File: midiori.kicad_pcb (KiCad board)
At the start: 2 copper layers, 140 x 150 mm, 47 parts, among them J1 x68000_expansion, J2 Conn_ARM_JTAG_SWD_10, J3 DIN-5_180degree, J4 Conn_02x03_Odd_Even, J7 AudioJack3, U1 74LCX07, U10 ICE40HX1K-VQ100, U11 TLV73333PDBV, U2 AT25SF081-SSHD-X, U3 TLV73312PDBV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

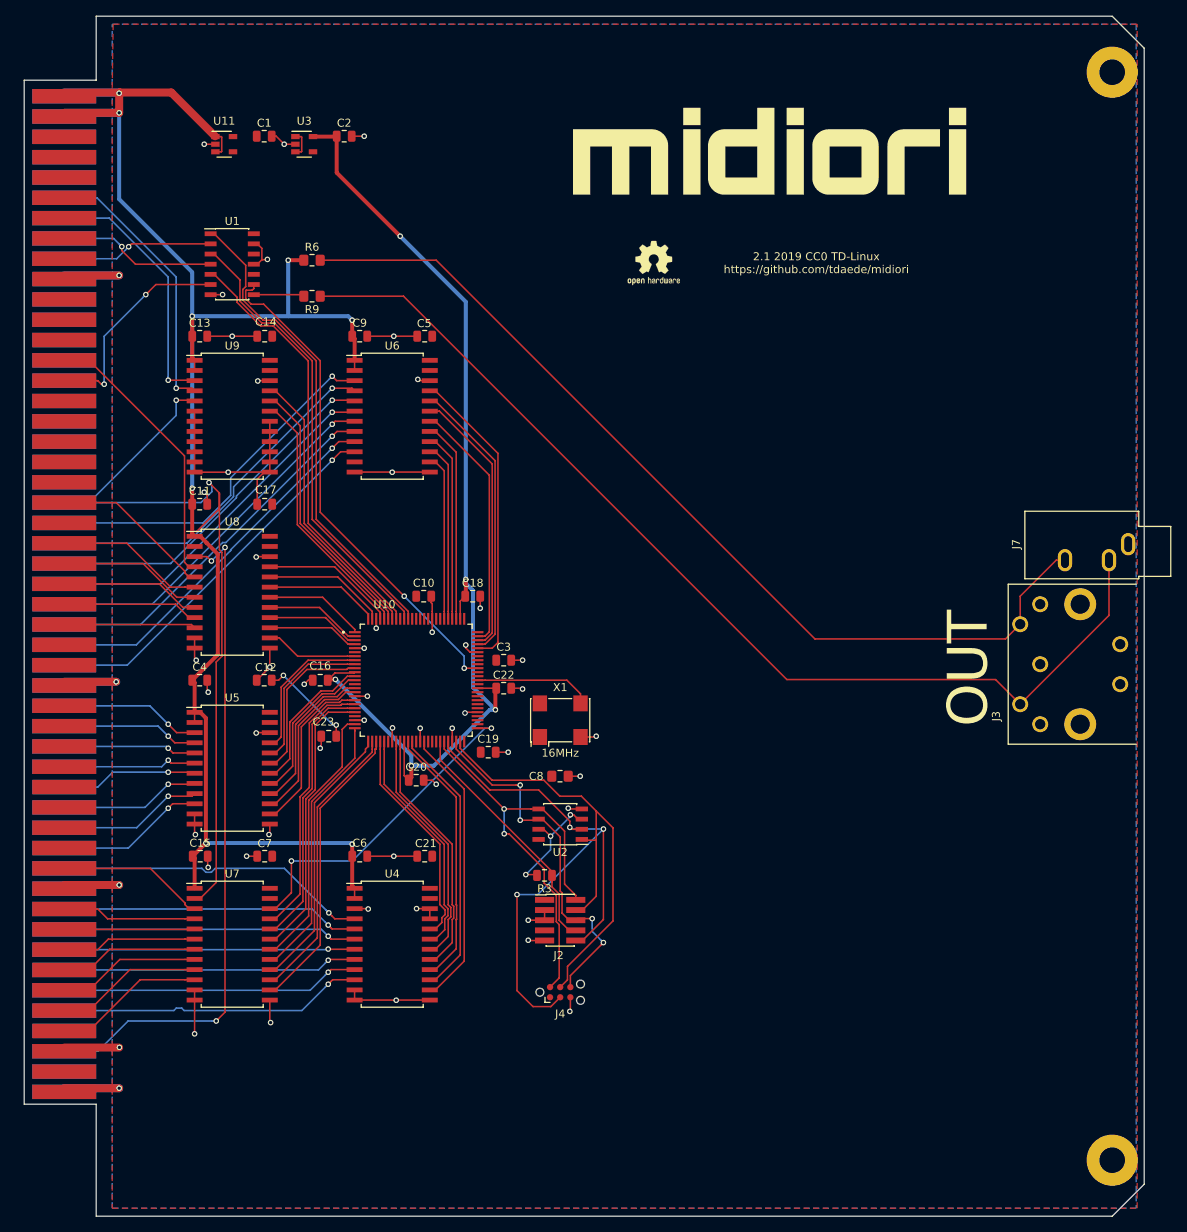
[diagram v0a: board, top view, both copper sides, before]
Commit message: PCB outline fixes
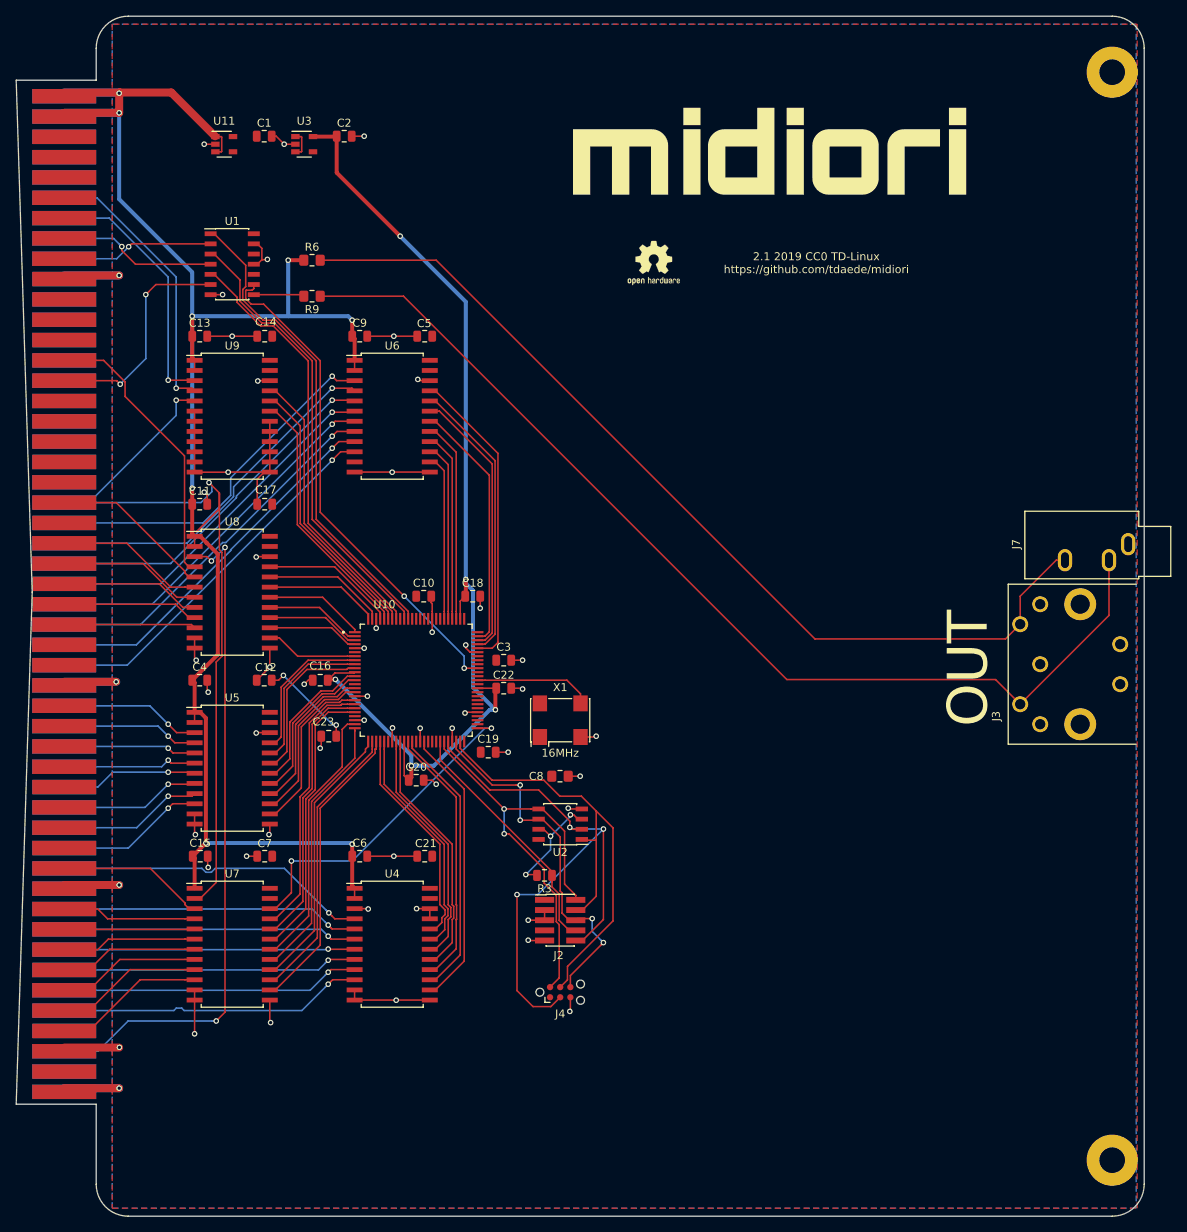
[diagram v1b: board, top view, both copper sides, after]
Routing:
- net +5V: track 222.5 -> 223.8 mm
- net /DTACK: track 27.2 -> 28.3 mm
- net /EXRESET: track 34.8 -> 35.9 mm
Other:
- board size 140 x 150 mm -> 141 x 150 mm

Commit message: set solder mask minimum width to 0
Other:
- rule pad_to_mask_clearance: 0.051 -> 0

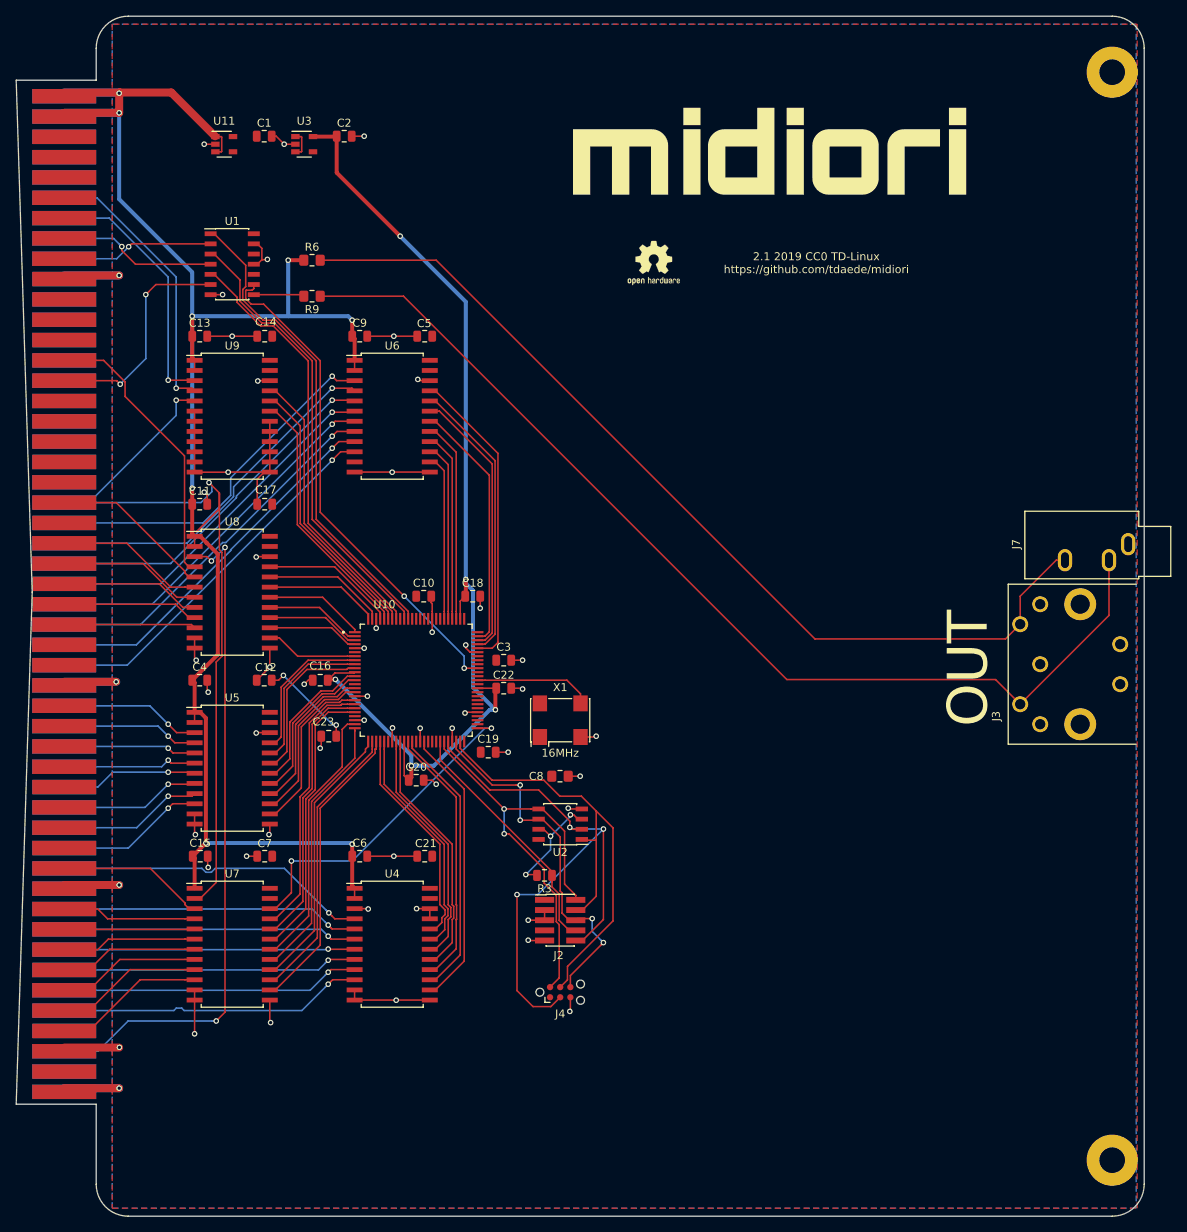
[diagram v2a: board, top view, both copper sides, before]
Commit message: add more connectors
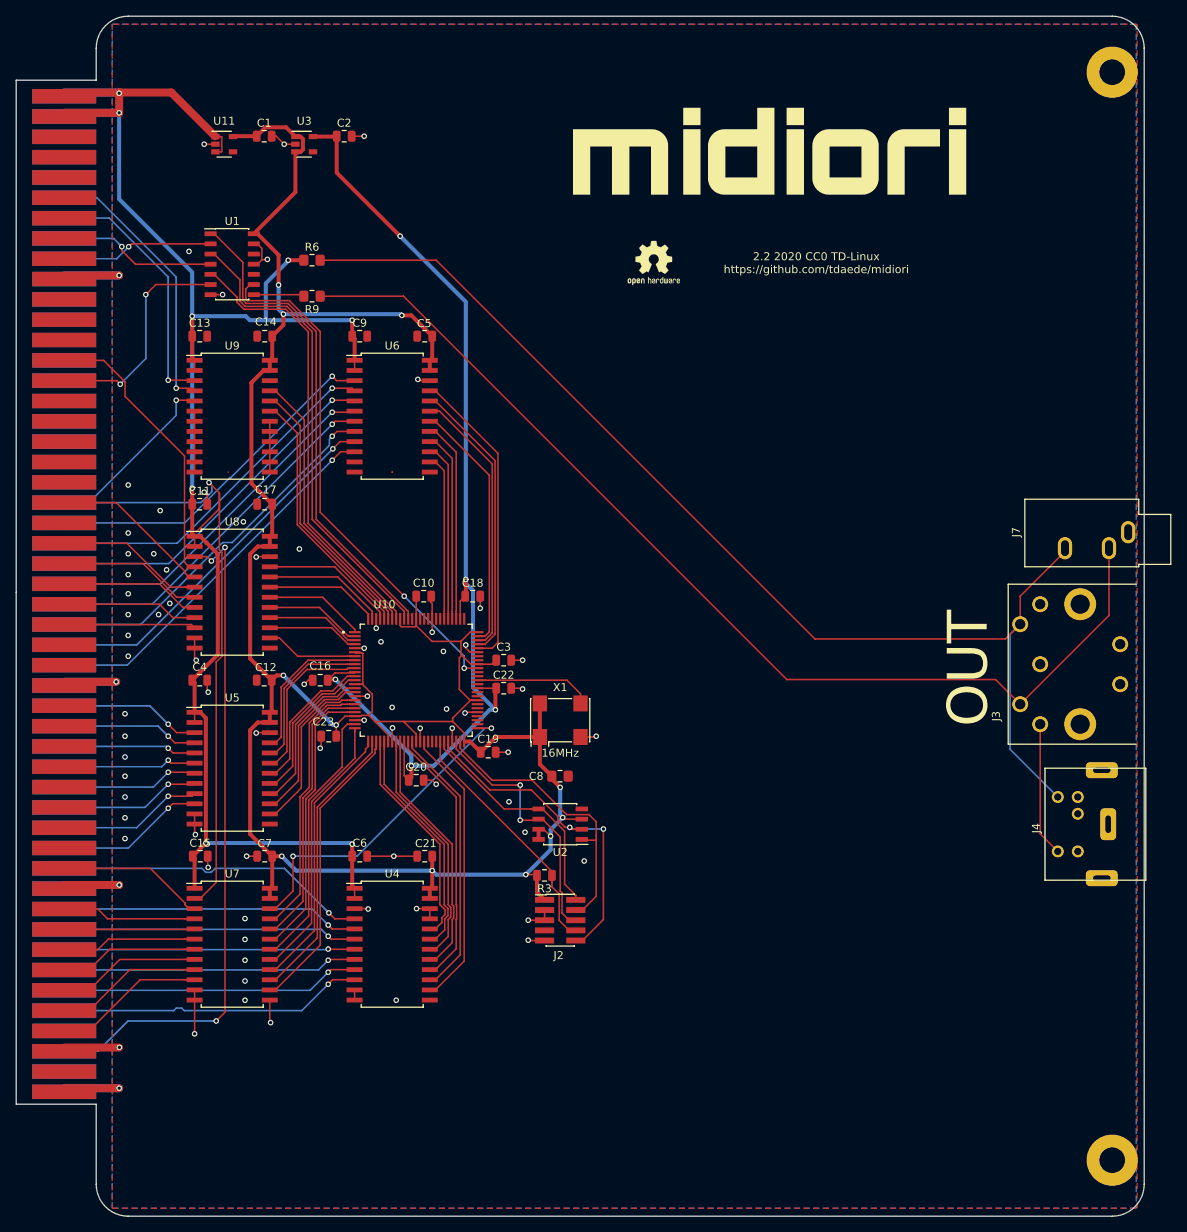
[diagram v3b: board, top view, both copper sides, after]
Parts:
- J4: value Conn_02x03_Odd_Even -> Mini-DIN-5; footprint Connector:Tag-Connect_TC2030-IDC-NL_2x03_P1.27mm_Vertical -> x68k:MD-50SM
- moved J4 71.6 mm to (180.5, 140.0), turned to -90 degrees
- moved J7 1.50 mm to (183.0, 103.5)
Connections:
- J4 pad 1: +3V3 -> Net-(J4-Pad1)
- J4 pad 2: /si -> GND
- J4 pad 3: /so -> Net-(J4-Pad3)
- J4 pad 4: /sck -> Net-(J3-Pad4)
- J4 pad 5: GND -> Net-(J3-Pad3)
- U10 pad 48: /ss -> /sck
- U10 pad 49: /sck -> /ss
- U2 pad 1: /sck -> /ss
- U2 pad 6: /ss -> /sck
- U9 pad 10: GND -> Net-(U9-Pad10)
- U9 pad 11: GND -> Net-(U9-Pad11)
- U9 pad 14: GND -> Net-(U9-Pad14)
- U9 pad 7: GND -> Net-(U9-Pad7)
- U9 pad 8: GND -> Net-(U9-Pad8)
- U9 pad 9: GND -> Net-(U9-Pad9)
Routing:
- net +3V3: track 30.4 -> 309.1 mm, vias 5 -> 11
- net GND: track 219.2 -> 161.6 mm, vias 55 -> 80
- net /so: track 75.2 -> 42.1 mm, vias 3 -> 2
- net /sck: track 62.5 -> 36.1 mm
- net /si: track 55.4 -> 29.4 mm, vias 2 -> 0
- net Net-(J3-Pad4): track 118.8 -> 144.3 mm
- net Net-(J3-Pad3): track 0.00 -> 16.8 mm
- net /ss: track 45.9 -> 33.2 mm, vias 4 -> 2
- net /dtack: track 53.9 -> 56.0 mm
- net /irq4: track 56.8 -> 58.9 mm
- net Net-(U1-Pad9): track 62.7 -> 64.7 mm
- net /irq2: track 59.9 -> 61.7 mm
- net +5V: track 223.8 -> 225.4 mm
- net /AB23: track 45.4 -> 44.1 mm
- net /AB22: track 45.2 -> 44.5 mm
- added copper zone on F.Cu, net GND
- removed copper zone on F.Cu, net +3V3
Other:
- outline, holes or cut-outs redrawn
- board text added: "2.2 2020 CC0 TD-Linux https://github.com/tdaede/midiori"
- board text removed: "2.1 2019 CC0 TD-Linux https://github.com/tdaede/midiori"

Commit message: one connector
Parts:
- removed J3: DIN-5_180degree, x68k:sds-50j
- removed J7: AudioJack3, Connector_Audio:Jack_3.5mm_CUI_SJ1-3533NG_Horizontal
- moved J4 16.9 mm to (180.4, 123.1)
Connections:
- J4 pad 5: Net-(J3-Pad3) -> Net-(J4-Pad5)
- R9 pad 1: Net-(J3-Pad5) -> Net-(J4-Pad5)
- U6 pad 11: Net-(U6-Pad11) -> GND
- U9 pad 10: Net-(U9-Pad10) -> GND
- U9 pad 11: Net-(U9-Pad11) -> GND
- U9 pad 14: Net-(U9-Pad14) -> GND
- U9 pad 7: Net-(U9-Pad7) -> GND
- U9 pad 8: Net-(U9-Pad8) -> GND
- U9 pad 9: Net-(U9-Pad9) -> GND
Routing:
- net Net-(J3-Pad5): track 131.2 -> 0.00 mm
- net Net-(J4-Pad5): track 0.00 -> 113.8 mm
- net Net-(J4-Pad4): track 144.3 -> 112.9 mm
- net Net-(J3-Pad3): track 16.8 -> 0.00 mm
- net /ss: track 33.2 -> 38.4 mm, vias 2 -> 0
- net /sck: track 36.1 -> 32.4 mm, vias 0 -> 2
- net /10MHz: track 85.0 -> 83.1 mm
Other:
- outline, holes or cut-outs redrawn

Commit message: more improvements
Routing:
- net GND: track 161.6 -> 166.7 mm, vias 80 -> 81
- net +5V: track 225.4 -> 227.3 mm
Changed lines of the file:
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@@
   )
   (setup
-    (last_trace_width 0.2)
+    (last_trace_width 1)
     (user_trace_width 0.5)
     (user_trace_width 1)
@@
   (gr_line (start 58 39) (end 181 39) (layer "Edge.Cuts") (width 0.05))
   (gr_line (start 185 43) (end 185 185) (layer "Edge.Cuts") (width 0.05))
+  (segment (start 57.6 48.6) (end 57.6 51.2) (width 1) (layer "F.Cu") (net 1))
+  (via (at 101.8 96.4) (size 0.7) (drill 0.4) (layers "F.Cu" "B.Cu") (net 2))
+  (segment (start 57.6 48.6) (end 63.485001 48.6) (width 1) (layer "F.Cu") (net 1))
+  (segment (start 63.485001 48.6) (end 68.9 54.014999) (width 1) (layer "F.Cu") (net 1))
+  (segment (start 57.6 48.6) (end 50.4 48.6) (width 1) (layer "F.Cu") (net 1))
+  (segment (start 50.4 48.6) (end 50 49) (width 1) (layer "F.Cu") (net 1))
+  (segment (start 57.6 48.6) (end 50.4 48.6) (width 1) (layer "B.Cu") (net 1))
+  (segment (start 50.4 48.6) (end 50 49) (width 1) (layer "B.Cu") (net 1))
+  (segment (start 66 70.8) (end 57.6 62.4) (width 0.5) (layer "B.Cu") (net 1))
+  (segment (start 66 76.5) (end 66 70.8) (width 0.5) (layer "B.Cu") (net 1))
+  (segment (start 57.6 62.4) (end 57.6 51) (width 0.5) (layer "B.Cu") (net 1))
+  (segment (start 50 51.2) (end 57.4 51.2) (width 1) (layer "F.Cu") (net 1))
+  (segment (start 50 51.2) (end 57.4 51.2) (width 1) (layer "B.Cu") (net 1))
+  (via (at 57.6 51.2) (size 0.7) (drill 0.4) (layers "F.Cu" "B.Cu") (net 1))
+  (via (at 57.6 71.6) (size 0.7) (drill 0.4) (layers "F.Cu" "B.Cu") (net 2))
+  (segment (start 50 71.6) (end 57.6 71.6) (width 1) (layer "B.Cu") (net 2))
+  (segment (start 50 71.6) (end 57.6 71.6) (width 1) (layer "F.Cu") (net 2))
+  (via (at 57.6 173.2) (size 0.7) (drill 0.4) (layers "F.Cu" "B.Cu") (net 2))
+  (segment (start 50 173.2) (end 57.6 173.2) (width 1) (layer "F.Cu") (net 2))
+  (segment (start 50 173.2) (end 57.6 173.2) (width 1) (layer "B.Cu") (net 2))
+  (segment (start 56.87 168) (end 57.6 168) (width 0.2) (layer "F.Cu") (net 2))
+  (via (at 57.6 168) (size 0.7) (drill 0.4) (layers "F.Cu" "B.Cu") (net 2))
+  (via (at 57.6 147.8) (size 0.7) (drill 0.4) (layers "F.Cu" "B.Cu") (net 2))
+  (segment (start 50 147.8) (end 57.6 147.8) (width 1) (layer "F.Cu") (net 2))
+  (segment (start 50 147.8) (end 57.6 147.8) (width 1) (layer "B.Cu") (net 2))
   (via (at 62 103.6) (size 0.7) (drill 0.4) (layers "F.Cu" "B.Cu") (net 2))
   (segment (start 65.16 102.34) (end 83.150001 84.349999) (width 0.2) (layer "B.Cu") (net 31))
@@
   (segment (start 174.1 119.7) (end 146.7 119.7) (width 0.2) (layer "F.Cu") (net 176))
   (segment (start 96.5 69.5) (end 82 69.5) (width 0.2) (layer "F.Cu") (net 176))
-  (segment (start 50 51.08) (end 56.87 51.08) (width 1) (layer "F.Cu") (net 1))
-  (segment (start 50 48.54) (end 56.87 48.54) (width 1) (layer "B.Cu") (net 1))
-  (segment (start 50 51.08) (end 56.87 51.08) (width 1) (layer "B.Cu") (net 1))
-  (segment (start 63.39 48.54) (end 68.864999 54.014999) (width 1) (layer "F.Cu") (net 1))
-  (segment (start 56.87 51.08) (end 56.87 48.63) (width 1) (layer "F.Cu") (net 1))
-  (segment (start 50 48.54) (end 56.96 48.54) (width 1) (layer "F.Cu") (net 1))
-  (segment (start 56.87 48.63) (end 56.96 48.54) (width 1) (layer "F.Cu") (net 1))
-  (segment (start 56.96 48.54) (end 63.39 48.54) (width 1) (layer "F.Cu") (net 1))
-  (via (at 56.87 48.63) (size 0.7) (drill 0.4) (layers "F.Cu" "B.Cu") (net 1))
-  (segment (start 56.87 48.54) (end 56.87 48.63) (width 1) (layer "B.Cu") (net 1))
-  (via (at 56.87 51.08) (size 0.7) (drill 0.4) (layers "F.Cu" "B.Cu") (net 1))
-  (segment (start 56.87 51.08) (end 56.87 61.87) (width 0.5) (layer "B.Cu") (net 1))
-  (segment (start 56.87 61.87) (end 66 71) (width 0.5) (layer "B.Cu") (net 1))
-  (segment (start 66 71) (end 66 76.5) (width 0.5) (layer "B.Cu") (net 1))
+  (via (at 57.6 48.6) (size 0.7) (drill 0.4) (layers "F.Cu" "B.Cu") (net 1))
   (segment (start 66 76.5) (end 66 79) (width 0.5) (layer "F.Cu") (net 1))
   (segment (start 66 81.715) (end 66.3 82.015) (width 0.5) (layer "F.Cu") (net 1))
@@
   (segment (start 69.690001 54.110001) (end 69.690001 55.889999) (width 0.2) (layer "F.Cu") (net 1))
   (segment (start 68.9 54.05) (end 69.63 54.05) (width 0.2) (layer "F.Cu") (net 1))
-  (segment (start 50 173.2) (end 56.87 173.2) (width 1) (layer "B.Cu") (net 2) (status 8000))
-  (segment (start 50 71.4) (end 56.87 71.4) (width 1) (layer "B.Cu") (net 2))
-  (segment (start 50 71.4) (end 56.87 71.4) (width 1) (layer "F.Cu") (net 2))
-  (segment (start 50 173.2) (end 56.87 173.2) (width 1) (layer "F.Cu") (net 2) (status 8000))
   (segment (start 50 168) (end 56.87 168) (width 1) (layer "F.Cu") (net 2) (status 8000))
   (segment (start 50 122.4) (end 56.5 122.4) (width 1) (layer "F.Cu") (net 2))
   (segment (start 50 122.4) (end 56.5 122.4) (width 1) (layer "B.Cu") (net 2))
-  (segment (start 50 147.8) (end 56.869916 147.8) (width 1) (layer "B.Cu") (net 2))
-  (segment (start 50 147.8) (end 56.869916 147.8) (width 1) (layer "F.Cu") (net 2))
   (via (at 89 115.5) (size 0.7) (drill 0.4) (layers "F.Cu" "B.Cu") (net 2))
   (segment (start 89 114.33) (end 89 115.5) (width 0.2) (layer "F.Cu") (net 2))
@@
   (via (at 87.9 124) (size 0.7) (drill 0.4) (layers "F.Cu" "B.Cu") (net 2))
   (segment (start 86.33 124) (end 87.9 124) (width 0.2) (layer "F.Cu") (net 2))
-  (via (at 56.87 71.4) (size 0.7) (drill 0.4) (layers "F.Cu" "B.Cu") (net 2))
   (via (at 57.6 122.4) (size 0.7) (drill 0.4) (layers "F.Cu" "B.Cu") (net 2))
-  (via (at 56.869916 147.8) (size 0.7) (drill 0.4) (layers "F.Cu" "B.Cu") (net 2))
-  (via (at 56.9 167.98) (size 0.7) (drill 0.4) (layers "F.Cu" "B.Cu") (net 2))
-  (segment (start 56.87 168) (end 56.88 168) (width 0.2) (layer "F.Cu") (net 2) (status 8000))
-  (segment (start 56.88 168) (end 56.9 167.98) (width 0.2) (layer "F.Cu") (net 2) (status 8000))
-  (via (at 56.87 173.2) (size 0.7) (drill 0.4) (layers "F.Cu" "B.Cu") (net 2))
   (segment (start 86.3 150.555) (end 87.955 150.555) (width 0.2) (layer "F.Cu") (net 2))
   (via (at 88 150.6) (size 0.7) (drill 0.4) (layers "F.Cu" "B.Cu") (net 2))
